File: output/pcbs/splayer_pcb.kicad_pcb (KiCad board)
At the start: 2 copper layers, 124.4 x 92.7 mm, 34 parts

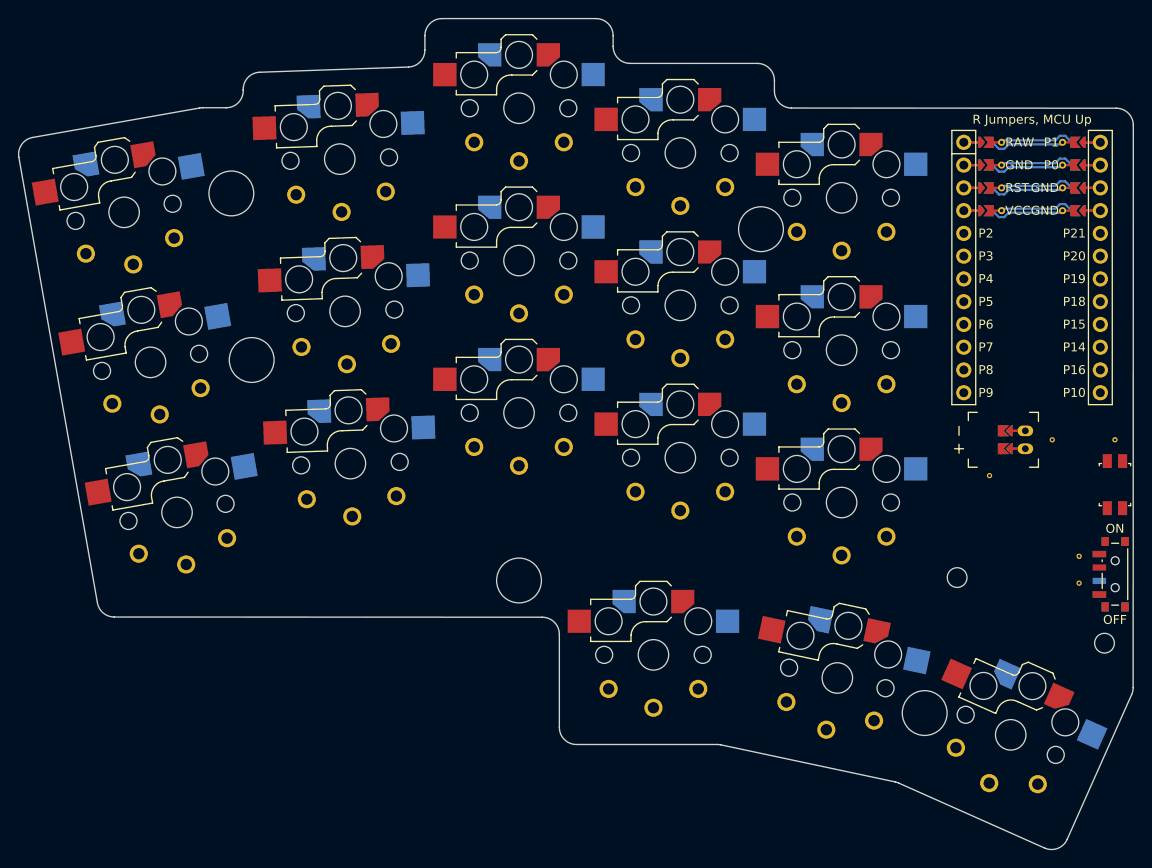
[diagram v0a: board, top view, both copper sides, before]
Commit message: drilled holes for reset side buttons
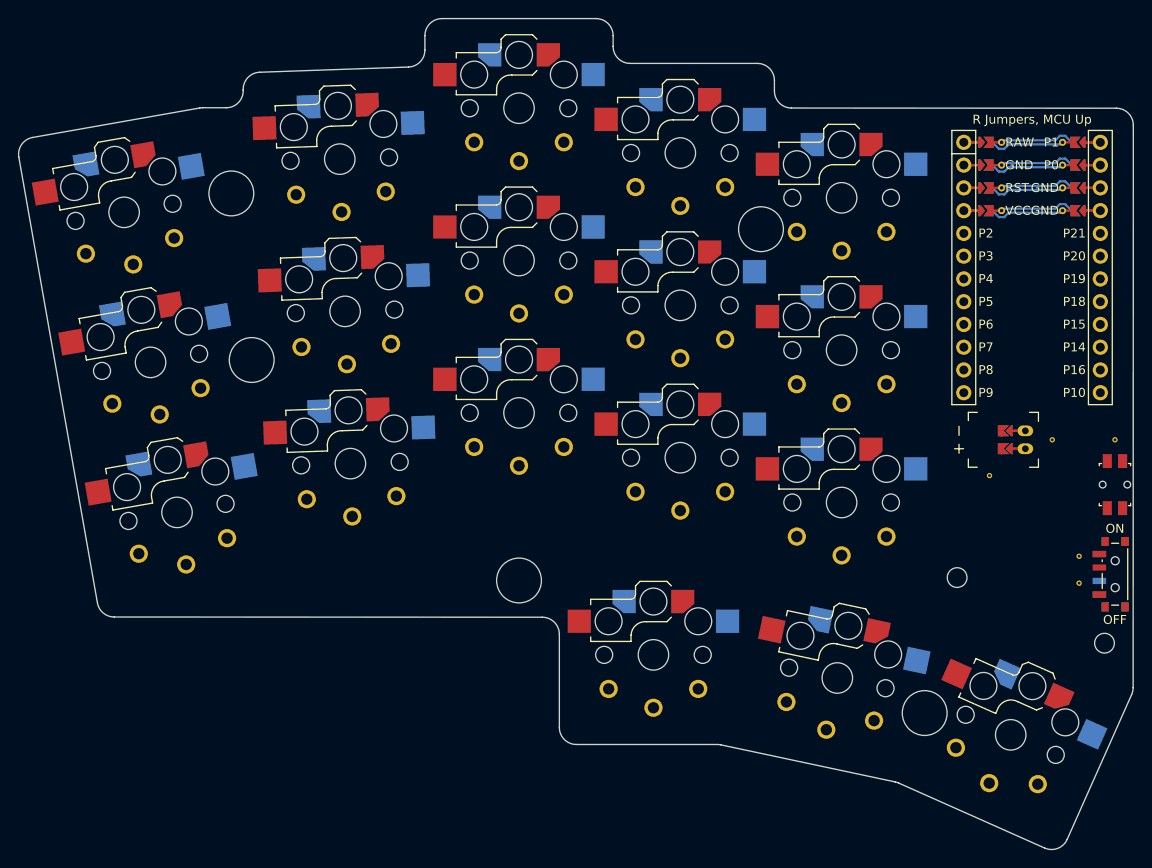
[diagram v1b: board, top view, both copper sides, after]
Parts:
- removed the REF** at (204.7, 91.9)
- removed the REF** at (190.7, 95.9)
- removed the REF** at (197.7, 91.9)
- removed the REF** at (200.7, 107.9)
- removed the REF** at (200.7, 104.9)
- added REF**: VIA-0.6mm, VIA-0.6mm, F.Cu at (204.7, 91.9)
- added REF**: VIA-0.6mm, VIA-0.6mm, F.Cu at (197.7, 91.9)
- added REF**: VIA-0.6mm, VIA-0.6mm, F.Cu at (200.7, 104.9)
- added REF**: VIA-0.6mm, VIA-0.6mm, F.Cu at (200.7, 107.9)
- added REF**: VIA-0.6mm, VIA-0.6mm, F.Cu at (190.7, 95.9)
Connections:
- S1 pad 2: GND -> P16
- S10 pad 2: GND -> P6
- S11 pad 2: GND -> P4
- S12 pad 2: GND -> P2
- S13 pad 2: GND -> P7
- S14 pad 2: GND -> P5
- S15 pad 2: GND -> P3
- S16 pad 2: GND -> P9
- S17 pad 2: GND -> P8
- S18 pad 2: GND -> P10
- S2 pad 2: GND -> P15
- S3 pad 2: GND -> P21
- S4 pad 2: GND -> P14
- S5 pad 2: GND -> P18
- S6 pad 2: GND -> P0
- S7 pad 2: GND -> P19
- S8 pad 2: GND -> P20
- S9 pad 2: GND -> P1
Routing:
- net (no net): track 0.00 -> 112.6 mm
- net GND: track 30.6 -> 0.00 mm
- net RAW: track 9.84 -> 0.00 mm
- net VCC: track 9.84 -> 0.00 mm
- net RST: track 9.84 -> 0.00 mm
- net P1: track 9.83 -> 0.00 mm
- net P0: track 9.83 -> 0.00 mm
- net MCU1_4: track 4.24 -> 0.00 mm
- net MCU1_3: track 4.24 -> 0.00 mm
- net MCU1_24: track 4.24 -> 0.00 mm
- net MCU1_23: track 4.24 -> 0.00 mm
- net MCU1_22: track 4.24 -> 0.00 mm
- net MCU1_21: track 4.24 -> 0.00 mm
- net MCU1_2: track 4.24 -> 0.00 mm
- net MCU1_1: track 4.24 -> 0.00 mm
